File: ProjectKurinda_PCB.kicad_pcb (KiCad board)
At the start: 2 copper layers, 30 x 105 mm, 9 parts, among them J1 JST PH, U1 ESP32-C3 SUPERMINI, U2 DHT11 T&H module, U3 Water sensor module, U4 SD3031 RTC module, U5 MPU6050 accelerometer module

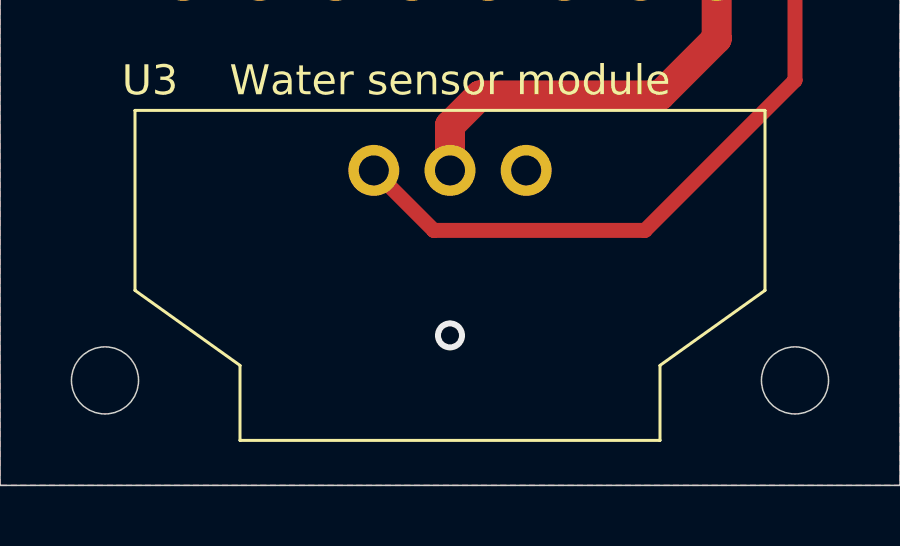
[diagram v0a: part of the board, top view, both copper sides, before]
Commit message: Added correct soil moisture sensor and updated silk screen to match.
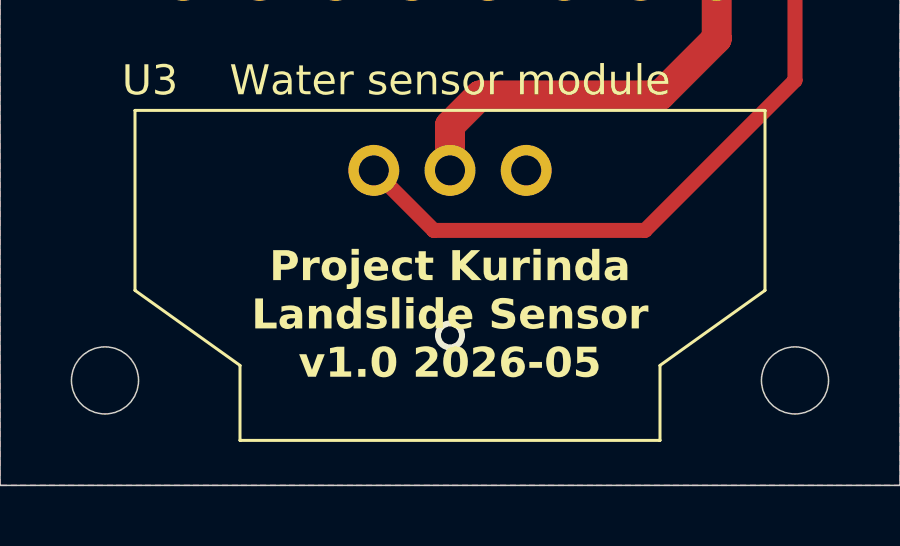
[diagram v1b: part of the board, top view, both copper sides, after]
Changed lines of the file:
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@@
 			(layer "F.SilkS")
+		)
+		(fp_rect
+			(start -12 -4)
+			(end 12 10)
+			(stroke
+				(width 0.1)
+				(type default)
+			)
+			(fill no)
+			(layer "B.SilkS")
+		)
+		(fp_rect
+			(start -12 -4)
+			(end 12 10)
+			(stroke
+				(width 0.05)
+				(type default)
+			)
+			(fill no)
+			(layer "B.CrtYd")
+		)
+		(fp_rect
+			(start -11 -3)
+			(end 11 9)
+			(stroke
+				(width 0.05)
+				(type default)
+			)
+			(fill no)
+			(layer "F.CrtYd")
 		)
 		(fp_text user "${REFERENCE}"
@@
 		(embedded_fonts no)
 		(model "${KIPRJMOD}/3D models/WaterSensor.step"
+			(hide yes)
 			(offset
 				(xyz 0 -25.35 0)
@@
 			(rotate
 				(xyz -90 -0 90)
+			)
+		)
+		(model "${KIPRJMOD}/3D models/Moisture Sensor.step"
+			(offset
+				(xyz 0 -45.8 -1.75)
+			)
+			(scale
+				(xyz 1 1 1)
+			)
+			(rotate
+				(xyz -90 -180 -0)
 			)
 		)
@@
 		(descr "MPU6050 breakout board")
 		(property "Reference" "U5"
-			(at 0 -3 0)
+			(at -12.5 14.75 0)
 			(unlocked yes)
 			(layer "B.SilkS")
@@
 		(layer "Edge.Cuts")
 	)
+	(gr_text "Project Kurinda\nLandslide Sensor\nv1.0 2026-05"
+		(at 70 146.5 0)
+		(layer "F.SilkS")
+		(effects
+			(font
+				(size 1 1)
+				(thickness 0.2)
+				(bold yes)
+			)
+			(justify bottom)
+		)
+	)
 	(gr_text "GND"
 		(at 68 47 0)
@@
 		)
 	)
-	(gr_text "Project Kurinda Landslide Sensor\nv1.0 2026-05"
-		(at 70 144 0)
-		(layer "B.SilkS")
-		(effects
-			(font
-				(size 1 1)
-				(thickness 0.2)
-				(bold yes)
-			)
-			(justify bottom mirror)
-		)
-	)
 	(via
 		(at 73.35 53)
@@
 	)
 	(segment
+		(start 62.38 55.72)
+		(end 64.22 55.72)
+		(width 0.5)
+		(layer "F.Cu")
+		(net "/SDA")
+	)
+	(segment
+		(start 70 60)
+		(end 70 78.5)
+		(width 0.5)
+		(layer "F.Cu")
+		(net "/SDA")
+	)
+	(segment
+		(start 67 57)
+		(end 70 60)
+		(width 0.5)
+		(layer "F.Cu")
+		(net "/SDA")
+	)
+	(segment
+		(start 64.22 55.72)
+		(end 65.5 57)
+		(width 0.5)
+		(layer "F.Cu")
+		(net "/SDA")
+	)
+	(segment
+		(start 65.5 57)
+		(end 67 57)
+		(width 0.5)
+		(layer "F.Cu")
+		(net "/SDA")
+	)
+	(segment
+		(start 64 84.5)
+		(end 64 125.73)
+		(width 0.5)
+		(layer "B.Cu")
+		(net "/SDA")
+	)
+	(segment
+		(start 64 125.73)
+		(end 71.27 133)
+		(width 0.5)
+		(layer "B.Cu")
+		(net "/SDA")
+	)
+	(segment
+		(start 70 78.5)
+		(end 64 84.5)
+		(width 0.5)
+		(layer "B.Cu")
+		(net "/SDA")
+	)
+	(segment
+		(start 65 124.19)
+		(end 65 86.04)
+		(width 0.5)
+		(layer "B.Cu")
+		(net "/SCL")
+	)
+	(segment
+		(start 72.54 68.42)
+		(end 72.54 78.5)
+		(width 0.5)
+		(layer "B.Cu")
+		(net "/SCL")
+	)
+	(segment
+		(start 65 86.04)
+		(end 72.54 78.5)
+		(width 0.5)
+		(layer "B.Cu")
+		(net "/SCL")
+	)
+	(segment
+		(start 62.38 58.26)
+		(end 72.54 68.42)
+		(width 0.5)
+		(layer "B.Cu")
+		(net "/SCL")
+	)
+	(segment
+		(start 73.81 133)
+		(end 65 124.19)
+		(width 0.5)
+		(layer "B.Cu")
+		(net "/SCL")
+	)
+	(segment
 		(start 67.46 63.96)
 		(end 64.3 60.8)
@@
 		(net "/RTC_INT")
 	)
-	(segment
-		(start 65 124.19)
-		(end 65 86.04)
-		(width 0.5)
-		(layer "B.Cu")
-		(net "/SCL")
-	)
-	(segment
-		(start 72.54 68.42)
-		(end 72.54 78.5)
-		(width 0.5)
-		(layer "B.Cu")
-		(net "/SCL")
-	)
-	(segment
-		(start 65 86.04)
-		(end 72.54 78.5)
-		(width 0.5)
-		(layer "B.Cu")
-		(net "/SCL")
-	)
-	(segment
-		(start 62.38 58.26)
-		(end 72.54 68.42)
-		(width 0.5)
-		(layer "B.Cu")
-		(net "/SCL")
-	)
-	(segment
-		(start 73.81 133)
-		(end 65 124.19)
-		(width 0.5)
-		(layer "B.Cu")
-		(net "/SCL")
-	)
-	(segment
-		(start 62.38 55.72)
-		(end 64.22 55.72)
-		(width 0.5)
-		(layer "F.Cu")
-		(net "/SDA")
-	)
-	(segment
-		(start 70 60)
-		(end 70 78.5)
-		(width 0.5)
-		(layer "F.Cu")
-		(net "/SDA")
-	)
-	(segment
-		(start 67 57)
-		(end 70 60)
-		(width 0.5)
-		(layer "F.Cu")
-		(net "/SDA")
-	)
-	(segment
-		(start 64.22 55.72)
-		(end 65.5 57)
-		(width 0.5)
-		(layer "F.Cu")
-		(net "/SDA")
-	)
-	(segment
-		(start 65.5 57)
-		(end 67 57)
-		(width 0.5)
-		(layer "F.Cu")
-		(net "/SDA")
-	)
-	(segment
-		(start 64 84.5)
-		(end 64 125.73)
-		(width 0.5)
-		(layer "B.Cu")
-		(net "/SDA")
-	)
-	(segment
-		(start 64 125.73)
-		(end 71.27 133)
-		(width 0.5)
-		(layer "B.Cu")
-		(net "/SDA")
-	)
-	(segment
-		(start 70 78.5)
-		(end 64 84.5)
-		(width 0.5)
-		(layer "B.Cu")
-		(net "/SDA")
-	)
 	(zone
